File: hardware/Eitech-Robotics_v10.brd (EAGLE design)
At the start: 70 x 50 mm, 144 parts, among them IC1 ATSAMW25-MR510PB, IC2 74LVC244PW, IC3 A3909-LY, IC4 A3909-LY, IC5 VREG-TS1117CW-3V3, IC6 AP65200-SP, J1 JST3-B3B-PH-K, J2 JST3-B3B-PH-K, J3 JST3-B3B-PH-K, J4 JST3-B3B-PH-K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

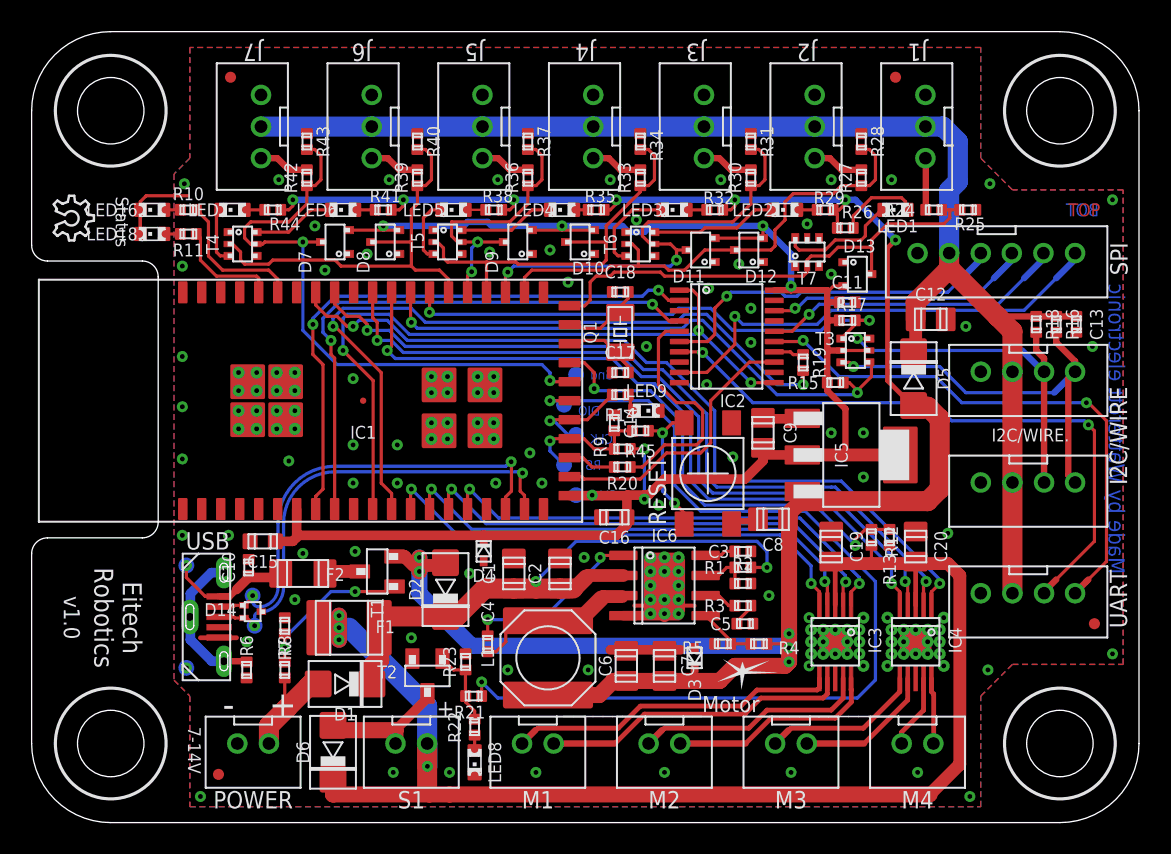
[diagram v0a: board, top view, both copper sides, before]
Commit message: updated schematics
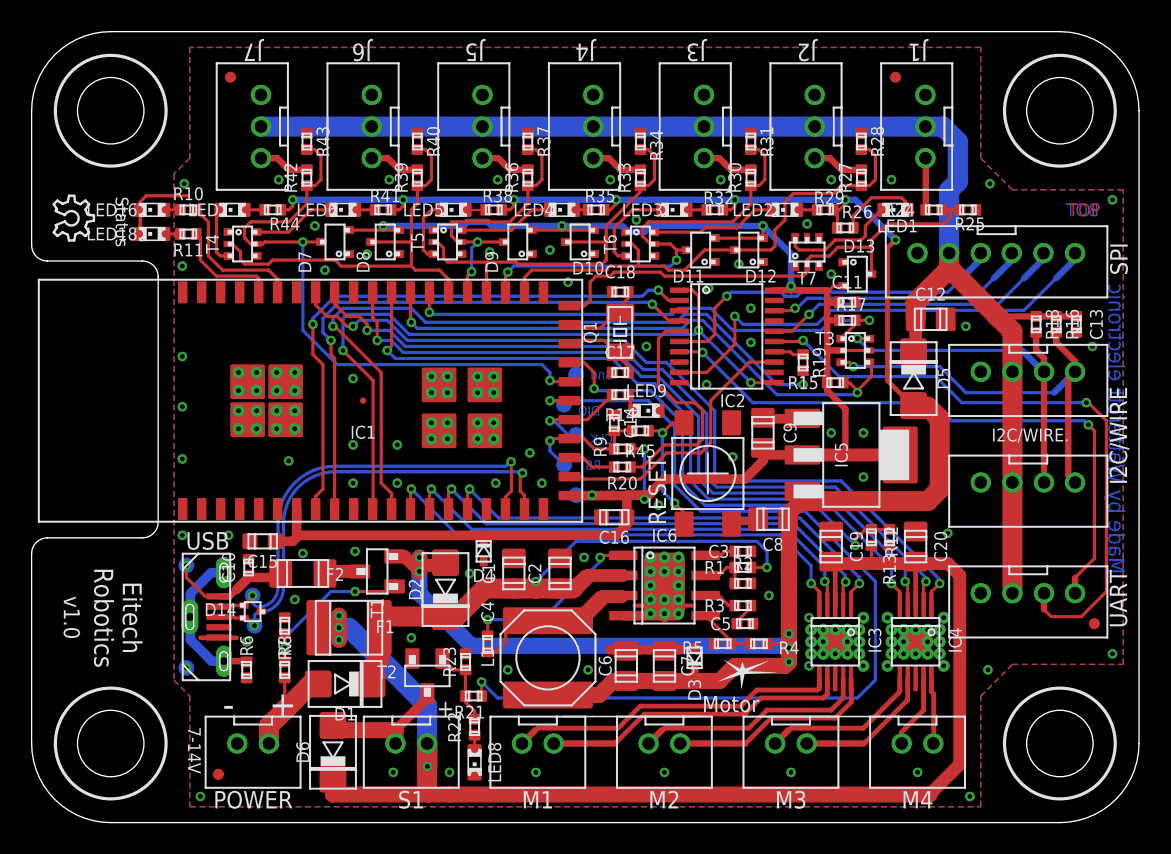
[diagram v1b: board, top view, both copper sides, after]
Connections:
- net RX_HV: now also UART.3; no longer UART.4
- net TX_HV: now also UART.4; no longer UART.3
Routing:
- net RX_HV: track 34.9 -> 39.8 mm
- net TX_HV: track 39.9 -> 39.1 mm
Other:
- board text added: "TX RX 5V GND"
- board text removed: "RX TX 5V GND"
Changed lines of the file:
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@@
 <layer number="51" name="tDocu" color="7" fill="1" visible="yes" active="yes"/>
 <layer number="52" name="bDocu" color="7" fill="1" visible="yes" active="yes"/>
-<layer number="53" name="tGND_GNDA" color="7" fill="9" visible="no" active="no"/>
-<layer number="54" name="bGND_GNDA" color="1" fill="9" visible="no" active="no"/>
-<layer number="56" name="wert" color="7" fill="1" visible="no" active="no"/>
-<layer number="57" name="tCAD" color="7" fill="1" visible="no" active="no"/>
-<layer number="60" name="Board" color="7" fill="1" visible="no" active="no"/>
 <layer number="90" name="Modules" color="5" fill="1" visible="no" active="no"/>
 <layer number="91" name="Nets" color="2" fill="1" visible="no" active="no"/>
@@
 <layer number="98" name="Guide" color="6" fill="1" visible="no" active="no"/>
 <layer number="99" name="SpiceOrder" color="5" fill="1" visible="no" active="no"/>
-<layer number="100" name="Muster" color="7" fill="1" visible="no" active="no"/>
-<layer number="105" name="Beschreib" color="9" fill="1" visible="no" active="no"/>
-<layer number="106" name="BGA-Top" color="4" fill="1" visible="no" active="no"/>
-<layer number="107" name="BD-Top" color="5" fill="1" visible="no" active="no"/>
-<layer number="153" name="FabDoc1" color="6" fill="1" visible="no" active="no"/>
-<layer number="154" name="FabDoc2" color="2" fill="1" visible="no" active="no"/>
-<layer number="155" name="FabDoc3" color="7" fill="15" visible="no" active="no"/>
-<layer number="200" name="200bmp" color="1" fill="10" visible="no" active="no"/>
-<layer number="217" name="217bmp" color="18" fill="1" visible="no" active="no"/>
-<layer number="218" name="218bmp" color="19" fill="1" visible="no" active="no"/>
-<layer number="219" name="219bmp" color="20" fill="1" visible="no" active="no"/>
-<layer number="220" name="220bmp" color="21" fill="1" visible="no" active="no"/>
-<layer number="221" name="221bmp" color="22" fill="1" visible="no" active="no"/>
-<layer number="222" name="222bmp" color="23" fill="1" visible="no" active="no"/>
-<layer number="223" name="223bmp" color="24" fill="1" visible="no" active="no"/>
-<layer number="224" name="224bmp" color="25" fill="1" visible="no" active="no"/>
-<layer number="250" name="Descript" color="3" fill="1" visible="no" active="no"/>
-<layer number="251" name="SMDround" color="12" fill="11" visible="no" active="no"/>
 </layers>
 <board>
@@
 <text x="66.421" y="38.735" size="0.8128" layer="16" font="vector" ratio="20" rot="MR0" align="center">BOT</text>
 <text x="66.548" y="38.735" size="0.8128" layer="1" font="vector" ratio="20" align="center">TOP</text>
-<wire x1="64.262" y1="12.192" x2="64.262" y2="11.557" width="0.13" layer="22"/>
-<wire x1="64.262" y1="11.557" x2="64.516" y2="11.938" width="0.13" layer="22"/>
-<wire x1="64.262" y1="11.557" x2="64.008" y2="11.938" width="0.13" layer="22"/>
-<wire x1="66.04" y1="12.192" x2="66.04" y2="11.557" width="0.13" layer="22"/>
-<wire x1="66.04" y1="12.192" x2="66.294" y2="11.811" width="0.13" layer="22"/>
-<wire x1="66.04" y1="12.192" x2="65.786" y2="11.811" width="0.13" layer="22"/>
+<wire x1="65.913" y1="12.192" x2="65.913" y2="11.557" width="0.13" layer="22"/>
+<wire x1="65.913" y1="11.557" x2="66.167" y2="11.938" width="0.13" layer="22"/>
+<wire x1="65.913" y1="11.557" x2="65.659" y2="11.938" width="0.13" layer="22"/>
+<wire x1="64.008" y1="12.192" x2="64.008" y2="11.557" width="0.13" layer="22"/>
+<wire x1="64.008" y1="12.192" x2="64.262" y2="11.811" width="0.13" layer="22"/>
+<wire x1="64.008" y1="12.192" x2="63.754" y2="11.811" width="0.13" layer="22"/>
 <text x="5.715" y="37.973" size="0.8128" layer="21" font="vector" ratio="15" rot="SR270" align="center">Status</text>
 <text x="5.461" y="12.954" size="1.2" layer="21" font="vector" ratio="15" rot="SR270" align="center">Eitech
@@
 <text x="60.96" y="34.417" size="0.61" layer="22" font="vector" ratio="15" rot="MR0" align="center">CS SCK MOSI MISO 5V GND</text>
 <text x="62.992" y="26.797" size="0.65" layer="22" font="vector" ratio="15" rot="MR0" align="center">SCL SDA 5V GND</text>
-<text x="62.738" y="12.827" size="0.65" layer="22" font="vector" ratio="15" rot="MR0" align="center">RX TX  5V GND</text>
+<text x="62.738" y="12.827" size="0.65" layer="22" font="vector" ratio="15" rot="MR0" align="center">TX RX 5V GND</text>
 <text x="62.992" y="19.812" size="0.65" layer="22" font="vector" ratio="15" rot="MR0" align="center">SCL SDA 5V GND</text>
 <text x="12.7" y="3.302" size="1.6764" layer="22" font="vector" ratio="15" rot="MR0" align="center">-</text>
@@
 </class>
 </classes>
-<designrules name="we-dru-2-layer *">
+<designrules name="we-dru-2-layer">
 <description language="de">&lt;b&gt;2 Layer PCB Design Rules&lt;/b&gt;</description>
 <description language="en">&lt;b&gt;2 Layer PCB Design Rules&lt;/b&gt;</description>
@@
 <param name="mdViaViaSameLayer" value="0.2mm"/>
 <param name="mnLayersViaInSmd" value="2"/>
-<param name="mdCopperDimension" value="0.5mm"/>
+<param name="mdCopperDimension" value="0.4mm"/>
 <param name="mdDrill" value="0.2mm"/>
 <param name="mdSmdStop" value="0mil"/>
@@
 <param name="rvMicroViaInner" value="0.25"/>
 <param name="rlMinPadTop" value="0.18mm"/>
-<param name="rlMaxPadTop" value="0.5mm"/>
+<param name="rlMaxPadTop" value="1mm"/>
 <param name="rlMinPadInner" value="0.18mm"/>
-<param name="rlMaxPadInner" value="0.5mm"/>
+<param name="rlMaxPadInner" value="1mm"/>
 <param name="rlMinPadBottom" value="0.18mm"/>
-<param name="rlMaxPadBottom" value="0.5mm"/>
-<param name="rlMinViaOuter" value="0.2mm"/>
-<param name="rlMaxViaOuter" value="0.5mm"/>
-<param name="rlMinViaInner" value="0.2mm"/>
-<param name="rlMaxViaInner" value="0.5mm"/>
+<param name="rlMaxPadBottom" value="1mm"/>
+<param name="rlMinViaOuter" value="0.16mm"/>
+<param name="rlMaxViaOuter" value="1mm"/>
+<param name="rlMinViaInner" value="0.16mm"/>
+<param name="rlMaxViaInner" value="1mm"/>
 <param name="rlMinMicroViaOuter" value="0.1mm"/>
 <param name="rlMaxMicroViaOuter" value="0.5mm"/>
@@
 <param name="srMinRoundness" value="0mil"/>
 <param name="srMaxRoundness" value="0mil"/>
-<param name="slThermalIsolate" value="0.2mm"/>
+<param name="slThermalIsolate" value="0.25mm"/>
 <param name="slThermalsForVias" value="0"/>
-<param name="dpMaxLengthDifference" value="2mm"/>
+<param name="dpMaxLengthDifference" value="5mm"/>
 <param name="dpGapFactor" value="2.5"/>
 <param name="checkGrid" value="0"/>
@@
 <via x="23.114" y="21.463" extent="1-16" drill="0.3"/>
 <via x="23.114" y="23.876" extent="1-16" drill="0.3"/>
+<wire x1="40.894" y1="13.716" x2="40.894" y2="14.097" width="0" layer="19" extent="1-1"/>
+<wire x1="39.116" y1="13.716" x2="39.116" y2="14.097" width="0" layer="19" extent="1-1"/>
 </signal>
 <signal name="N$11">
@@
 <signal name="RX_HV">
 <contactref element="IC2" pad="15"/>
-<wire x1="66.802" y1="15.367" x2="67.945" y2="16.51" width="0.2032" layer="1"/>
-<wire x1="67.945" y1="16.51" x2="67.945" y2="25.4" width="0.2032" layer="1"/>
+<wire x1="67.945" y1="14.605" x2="67.945" y2="25.4" width="0.2032" layer="1"/>
 <wire x1="67.945" y1="25.4" x2="66.802" y2="26.543" width="0.2032" layer="1"/>
 <wire x1="66.802" y1="26.543" x2="66.675" y2="26.543" width="0.2032" layer="1"/>
@@
 <wire x1="48.697" y1="30.409" x2="46.942" y2="30.409" width="0.2032" layer="1"/>
 <wire x1="51.054" y1="28.194" x2="48.768" y2="30.48" width="0.2032" layer="16"/>
-<contactref element="UART" pad="4"/>
-<wire x1="65.96" y1="14.5" x2="65.96" y2="14.525" width="0.4064" layer="1"/>
-<wire x1="65.96" y1="14.525" x2="66.675" y2="15.24" width="0.4064" layer="1"/>
-<wire x1="66.675" y1="15.24" x2="66.802" y2="15.367" width="0.4064" layer="1"/>
+<contactref element="UART" pad="3"/>
+<wire x1="67.945" y1="14.605" x2="66.3575" y2="13.0175" width="0.2032" layer="1"/>
+<wire x1="66.3575" y1="13.0175" x2="64.4525" y2="13.0175" width="0.2032" layer="1"/>
+<wire x1="64" y1="14.5" x2="64" y2="13.47" width="0.4064" layer="1"/>
+<wire x1="64.4525" y1="13.0175" x2="64" y2="13.47" width="0.2032" layer="1"/>
 </signal>
 <signal name="TX_HV">
 <contactref element="IC2" pad="7"/>
-<wire x1="67.183" y1="17.78" x2="67.183" y2="24.765" width="0.2032" layer="1"/>
+<wire x1="67.183" y1="16.7005" x2="67.183" y2="24.765" width="0.2032" layer="1"/>
 <wire x1="67.183" y1="24.765" x2="66.802" y2="25.146" width="0.2032" layer="1"/>
 <via x="66.802" y="25.146" extent="1-16" drill="0.3"/>
@@
 <wire x1="42.418" y1="29.718" x2="42.377" y2="29.759" width="0.2032" layer="1"/>
 <wire x1="42.377" y1="29.759" x2="40.942" y2="29.759" width="0.2032" layer="1"/>
-<contactref element="UART" pad="3"/>
-<wire x1="64" y1="14.5" x2="64" y2="14.597" width="0.4064" layer="1"/>
-<wire x1="64" y1="14.597" x2="64.77" y2="15.367" width="0.4064" layer="1"/>
-<wire x1="64.77" y1="15.367" x2="67.183" y2="17.78" width="0.2032" layer="1"/>
+<contactref element="UART" pad="4"/>
+<wire x1="65.96" y1="14.5" x2="65.96" y2="15.4775" width="0.4064" layer="1"/>
+<wire x1="67.183" y1="16.7005" x2="65.96" y2="15.4775" width="0.2032" layer="1"/>
 </signal>
 <signal name="MISO_HV">
@@
 <contactref element="D5" pad="C"/>
 <wire x1="55.8825" y1="31.8135" x2="55.8825" y2="29.955" width="0.8128" layer="1"/>
-<wire x1="55.8825" y1="29.955" x2="55.753" y2="29.767" width="0.8128" layer="1"/>
+<wire x1="55.8825" y1="29.955" x2="55.8825" y2="29.8965" width="0.2032" layer="1"/>
+<wire x1="55.8825" y1="29.8965" x2="55.753" y2="29.767" width="0.2032" layer="1"/>
 </signal>
 <signal name="N$2">
